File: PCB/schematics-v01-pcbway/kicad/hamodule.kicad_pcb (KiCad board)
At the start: 2 copper layers, 78 x 82.1 mm, 157 parts, among them J1 Conn_01x05_Female, J2 Conn_01x05_Female

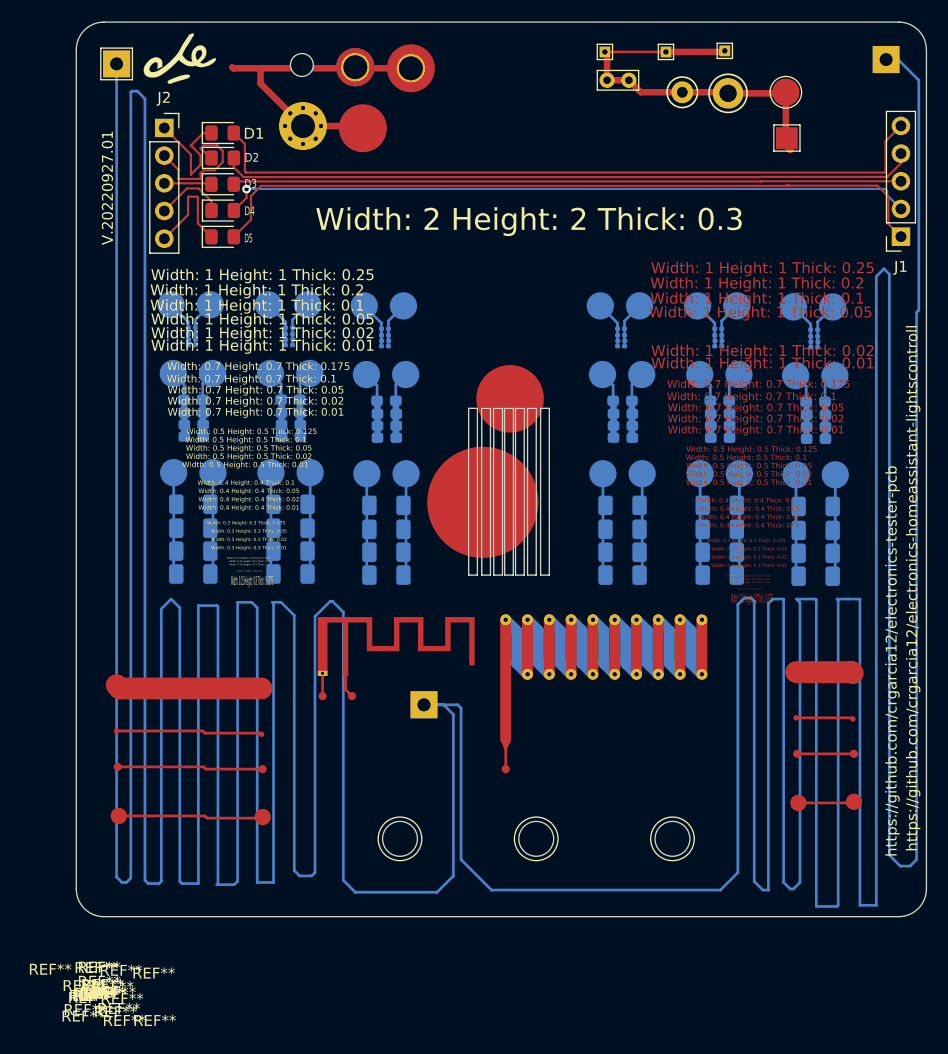
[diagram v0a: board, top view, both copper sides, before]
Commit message: removing **REF**
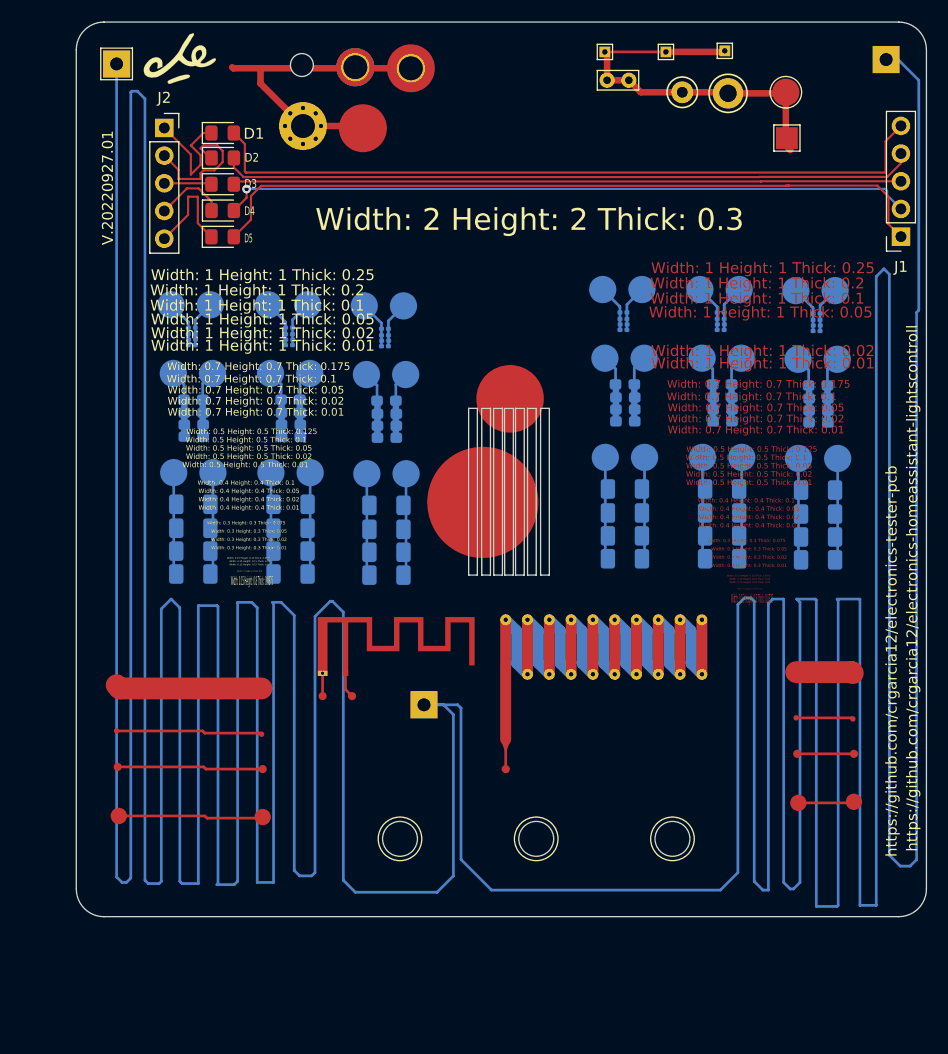
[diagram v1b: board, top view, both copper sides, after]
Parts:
- removed the REF** at (97.8, 77.1)
- removed the REF** at (81.9, 62.8)
- removed the REF** at (89.1, 67.5)
- removed the REF** at (81.9, 71.9)
- removed the REF** at (90.6, 56.5)
- removed the REF** at (80.0, 60.2)
- removed the REF** at (97.7, 59.8)
- removed the REF** at (88.9, 59.2)
- removed the REF** at (80.2, 67.5)
- removed the REF** at (81.7, 56.5)
- removed the REF** at (99.6, 62.9)
- removed the REF** at (87.2, 71.9)
- removed the REF** at (78.3, 71.9)
- removed the REF** at (89.1, 66.4)
- removed the REF** at (90.8, 71.9)
- removed the REF** at (90.8, 62.8)
- removed the REF** at (99.6, 72.0)
- removed the REF** at (96.0, 62.9)
- removed the REF** at (88.9, 58.6)
- removed the REF** at (97.7, 60.3)
- removed the REF** at (80.2, 68.6)
- removed the REF** at (89.0, 79.1)
- removed the REF** at (97.9, 68.7)
- removed the REF** at (97.8, 81.3)
- removed the REF** at (97.9, 67.6)
- removed the REF** at (80.1, 79.1)
- removed the REF** at (78.1, 56.5)
- removed the REF** at (88.9, 59.7)
- removed the REF** at (88.9, 60.2)
- removed the REF** at (80.1, 65.2)
- removed the REF** at (80.1, 77.0)
- removed the REF** at (87.2, 62.8)
- removed the REF** at (89.0, 77.0)
- removed the REF** at (89.0, 81.2)
- removed the REF** at (97.9, 66.5)
- removed the REF** at (99.4, 56.6)
- removed the REF** at (97.8, 65.3)
- removed the REF** at (97.7, 59.3)
- removed the REF** at (97.7, 58.7)
- removed the REF** at (80.1, 74.8)
- removed the REF** at (96.0, 72.0)
- removed the REF** at (89.1, 68.6)
- removed the REF** at (89.0, 74.8)
- removed the REF** at (80.0, 59.2)
- removed the REF** at (87.0, 56.5)
- removed the REF** at (97.8, 74.9)
- removed the REF** at (80.2, 66.4)
- removed the REF** at (97.8, 79.2)
- removed the REF** at (95.8, 56.6)
- removed the REF** at (78.3, 62.8)
- removed the REF** at (89.0, 65.2)
- removed the REF** at (80.0, 58.6)
- removed the REF** at (80.0, 59.7)
- removed the REF** at (80.1, 81.2)
- added REF**: C_0201_0603Metric, Capacitor_SMD:C_0201_0603Metric, B.Cu at (97.9, 57.2)
- added REF**: C_1206_3216Metric_Pad1.33x1.80mm_HandSolder, Capacitor_SMD:C_1206_3216Metric_Pad1.33x1.80mm_HandSolder, B.Cu at (98.1, 73.4)
- added REF**: TestPoint_Pad_D2.5mm, TestPoint:TestPoint_Pad_D2.5mm, B.Cu at (96.3, 70.5)
- added REF**: C_1206_3216Metric_Pad1.33x1.80mm_HandSolder, Capacitor_SMD:C_1206_3216Metric_Pad1.33x1.80mm_HandSolder, B.Cu at (98.1, 77.7)
- added REF**: C_0603_1608Metric_Pad1.08x0.95mm_HandSolder, Capacitor_SMD:C_0603_1608Metric_Pad1.08x0.95mm_HandSolder, B.Cu at (89.3, 67.1)
- added REF**: C_0603_1608Metric_Pad1.08x0.95mm_HandSolder, Capacitor_SMD:C_0603_1608Metric_Pad1.08x0.95mm_HandSolder, B.Cu at (89.3, 64.9)
- added REF**: C_0201_0603Metric, Capacitor_SMD:C_0201_0603Metric, B.Cu at (89.1, 57.1)
- added REF**: C_0201_0603Metric, Capacitor_SMD:C_0201_0603Metric, B.Cu at (97.9, 57.8)
- added REF**: C_0603_1608Metric_Pad1.08x0.95mm_HandSolder, Capacitor_SMD:C_0603_1608Metric_Pad1.08x0.95mm_HandSolder, B.Cu at (80.4, 67.1)
- added REF**: TestPoint_Pad_D2.5mm, TestPoint:TestPoint_Pad_D2.5mm, B.Cu at (99.6, 55.1)
- added REF**: C_1206_3216Metric_Pad1.33x1.80mm_HandSolder, Capacitor_SMD:C_1206_3216Metric_Pad1.33x1.80mm_HandSolder, B.Cu at (80.3, 77.6)
- added REF**: TestPoint_Pad_D2.5mm, TestPoint:TestPoint_Pad_D2.5mm, B.Cu at (82.1, 61.3)
- added REF**: C_0603_1608Metric_Pad1.08x0.95mm_HandSolder, Capacitor_SMD:C_0603_1608Metric_Pad1.08x0.95mm_HandSolder, B.Cu at (98.1, 65.0)
- added REF**: C_0603_1608Metric_Pad1.08x0.95mm_HandSolder, Capacitor_SMD:C_0603_1608Metric_Pad1.08x0.95mm_HandSolder, B.Cu at (89.3, 66.0)
- added REF**: C_0201_0603Metric, Capacitor_SMD:C_0201_0603Metric, B.Cu at (89.1, 58.7)
- added REF**: C_0603_1608Metric_Pad1.08x0.95mm_HandSolder, Capacitor_SMD:C_0603_1608Metric_Pad1.08x0.95mm_HandSolder, B.Cu at (80.4, 66.0)
- added REF**: C_0603_1608Metric_Pad1.08x0.95mm_HandSolder, Capacitor_SMD:C_0603_1608Metric_Pad1.08x0.95mm_HandSolder, B.Cu at (98.1, 67.2)
- added REF**: TestPoint_Pad_D2.5mm, TestPoint:TestPoint_Pad_D2.5mm, B.Cu at (96.2, 61.4)
- added REF**: C_1206_3216Metric_Pad1.33x1.80mm_HandSolder, Capacitor_SMD:C_1206_3216Metric_Pad1.33x1.80mm_HandSolder, B.Cu at (98.1, 75.6)
- added REF**: C_0603_1608Metric_Pad1.08x0.95mm_HandSolder, Capacitor_SMD:C_0603_1608Metric_Pad1.08x0.95mm_HandSolder, B.Cu at (80.3, 63.7)
- added REF**: C_0201_0603Metric, Capacitor_SMD:C_0201_0603Metric, B.Cu at (80.2, 57.1)
- added REF**: C_0201_0603Metric, Capacitor_SMD:C_0201_0603Metric, B.Cu at (80.2, 58.7)
- added REF**: C_1206_3216Metric_Pad1.33x1.80mm_HandSolder, Capacitor_SMD:C_1206_3216Metric_Pad1.33x1.80mm_HandSolder, B.Cu at (89.3, 79.7)
- added REF**: TestPoint_Pad_D2.5mm, TestPoint:TestPoint_Pad_D2.5mm, B.Cu at (99.9, 70.5)
- added REF**: C_1206_3216Metric_Pad1.33x1.80mm_HandSolder, Capacitor_SMD:C_1206_3216Metric_Pad1.33x1.80mm_HandSolder, B.Cu at (80.3, 75.5)
- added REF**: C_0603_1608Metric_Pad1.08x0.95mm_HandSolder, Capacitor_SMD:C_0603_1608Metric_Pad1.08x0.95mm_HandSolder, B.Cu at (80.4, 64.9)
- added REF**: TestPoint_Pad_D2.5mm, TestPoint:TestPoint_Pad_D2.5mm, B.Cu at (90.8, 55.0)
- added REF**: TestPoint_Pad_D2.5mm, TestPoint:TestPoint_Pad_D2.5mm, B.Cu at (87.2, 55.0)
- added REF**: TestPoint_Pad_D2.5mm, TestPoint:TestPoint_Pad_D2.5mm, B.Cu at (82.1, 70.4)
- added REF**: TestPoint_Pad_D2.5mm, TestPoint:TestPoint_Pad_D2.5mm, B.Cu at (87.4, 61.3)
- added REF**: C_0603_1608Metric_Pad1.08x0.95mm_HandSolder, Capacitor_SMD:C_0603_1608Metric_Pad1.08x0.95mm_HandSolder, B.Cu at (98.1, 63.8)
- added REF**: TestPoint_Pad_D2.5mm, TestPoint:TestPoint_Pad_D2.5mm, B.Cu at (96.0, 55.1)
- added REF**: C_0201_0603Metric, Capacitor_SMD:C_0201_0603Metric, B.Cu at (97.9, 58.3)
- added REF**: C_0201_0603Metric, Capacitor_SMD:C_0201_0603Metric, B.Cu at (80.2, 58.2)
- added REF**: C_1206_3216Metric_Pad1.33x1.80mm_HandSolder, Capacitor_SMD:C_1206_3216Metric_Pad1.33x1.80mm_HandSolder, B.Cu at (98.1, 79.8)
- added REF**: C_1206_3216Metric_Pad1.33x1.80mm_HandSolder, Capacitor_SMD:C_1206_3216Metric_Pad1.33x1.80mm_HandSolder, B.Cu at (80.3, 79.7)
- added REF**: C_1206_3216Metric_Pad1.33x1.80mm_HandSolder, Capacitor_SMD:C_1206_3216Metric_Pad1.33x1.80mm_HandSolder, B.Cu at (89.3, 73.3)
- added REF**: TestPoint_Pad_D2.5mm, TestPoint:TestPoint_Pad_D2.5mm, B.Cu at (78.5, 61.3)
- added REF**: C_0603_1608Metric_Pad1.08x0.95mm_HandSolder, Capacitor_SMD:C_0603_1608Metric_Pad1.08x0.95mm_HandSolder, B.Cu at (98.1, 66.1)
- added REF**: TestPoint_Pad_D2.5mm, TestPoint:TestPoint_Pad_D2.5mm, B.Cu at (87.5, 70.4)
- added REF**: TestPoint_Pad_D2.5mm, TestPoint:TestPoint_Pad_D2.5mm, B.Cu at (78.3, 55.0)
- added REF**: TestPoint_Pad_D2.5mm, TestPoint:TestPoint_Pad_D2.5mm, B.Cu at (91.1, 70.4)
- added REF**: C_0603_1608Metric_Pad1.08x0.95mm_HandSolder, Capacitor_SMD:C_0603_1608Metric_Pad1.08x0.95mm_HandSolder, B.Cu at (89.3, 63.7)
- added REF**: TestPoint_Pad_D2.5mm, TestPoint:TestPoint_Pad_D2.5mm, B.Cu at (99.8, 61.4)
- added REF**: TestPoint_Pad_D2.5mm, TestPoint:TestPoint_Pad_D2.5mm, B.Cu at (78.5, 70.4)
- added REF**: C_0201_0603Metric, Capacitor_SMD:C_0201_0603Metric, B.Cu at (89.1, 57.7)
- added REF**: TestPoint_Pad_D2.5mm, TestPoint:TestPoint_Pad_D2.5mm, B.Cu at (91.0, 61.3)
- added REF**: C_0201_0603Metric, Capacitor_SMD:C_0201_0603Metric, B.Cu at (97.9, 58.8)
- added REF**: C_1206_3216Metric_Pad1.33x1.80mm_HandSolder, Capacitor_SMD:C_1206_3216Metric_Pad1.33x1.80mm_HandSolder, B.Cu at (80.3, 73.3)
- added REF**: C_1206_3216Metric_Pad1.33x1.80mm_HandSolder, Capacitor_SMD:C_1206_3216Metric_Pad1.33x1.80mm_HandSolder, B.Cu at (89.3, 75.5)
- added REF**: C_0201_0603Metric, Capacitor_SMD:C_0201_0603Metric, B.Cu at (89.1, 58.2)
- added REF**: C_1206_3216Metric_Pad1.33x1.80mm_HandSolder, Capacitor_SMD:C_1206_3216Metric_Pad1.33x1.80mm_HandSolder, B.Cu at (89.3, 77.6)
- added REF**: C_0201_0603Metric, Capacitor_SMD:C_0201_0603Metric, B.Cu at (80.2, 57.7)
- added REF**: TestPoint_Pad_D2.5mm, TestPoint:TestPoint_Pad_D2.5mm, B.Cu at (81.9, 55.0)
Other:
- board text removed: "REF**"
